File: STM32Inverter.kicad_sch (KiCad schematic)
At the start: 12 parts, among them U1 STM32F303VCTx, Y1 16MHz

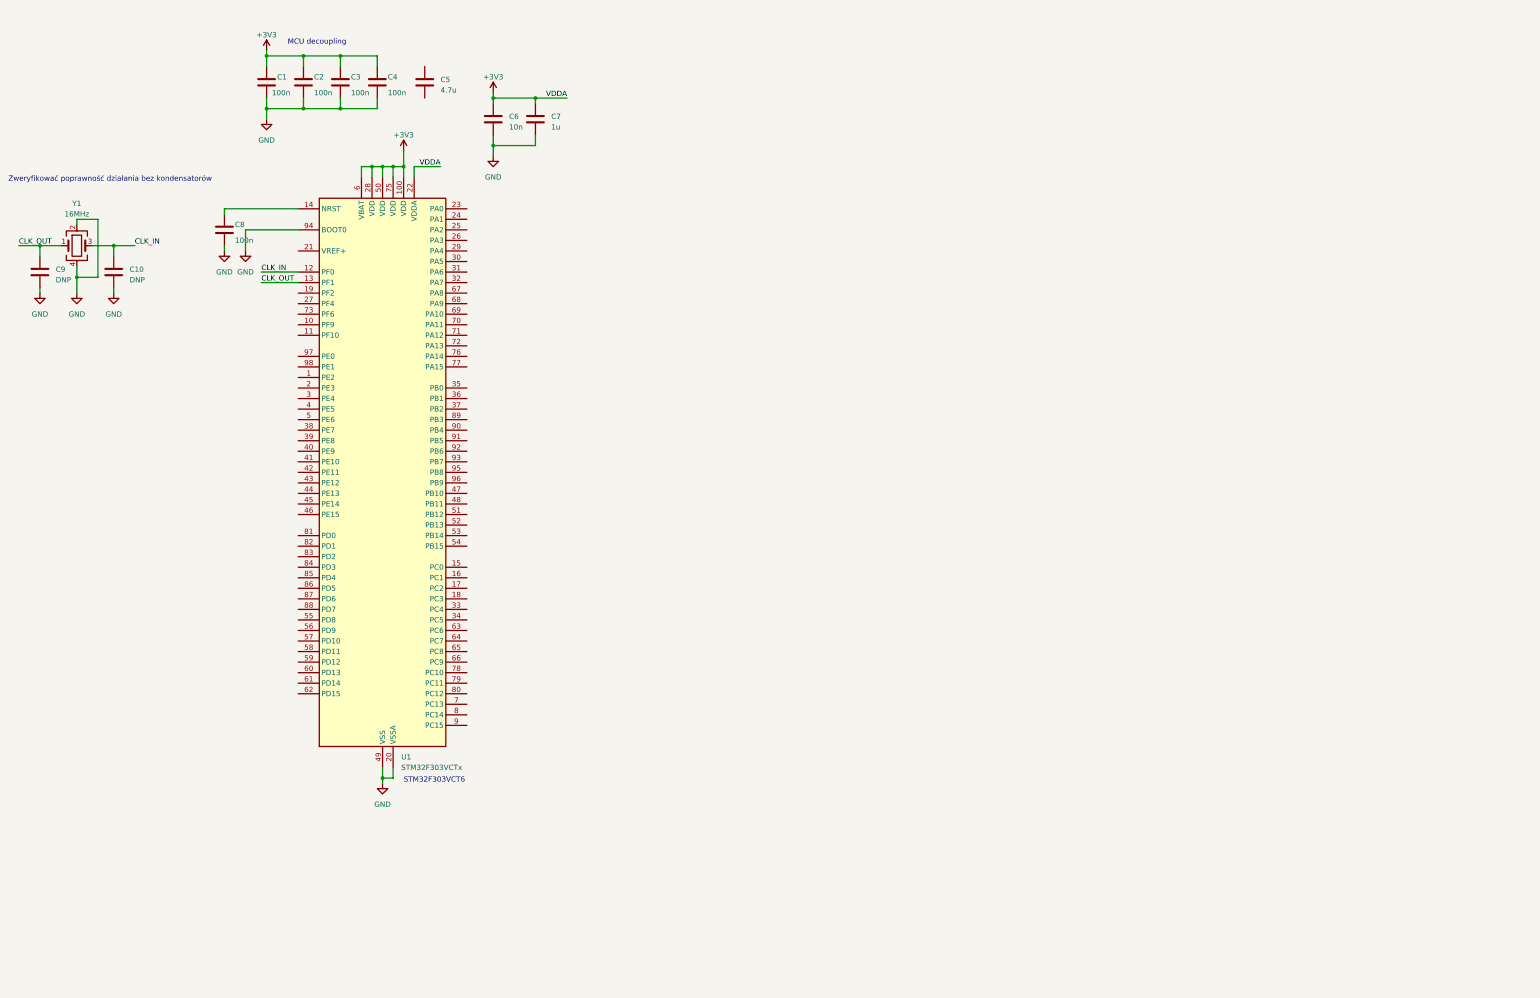
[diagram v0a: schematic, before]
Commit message: Added STM32Cube file and schematic subsheets
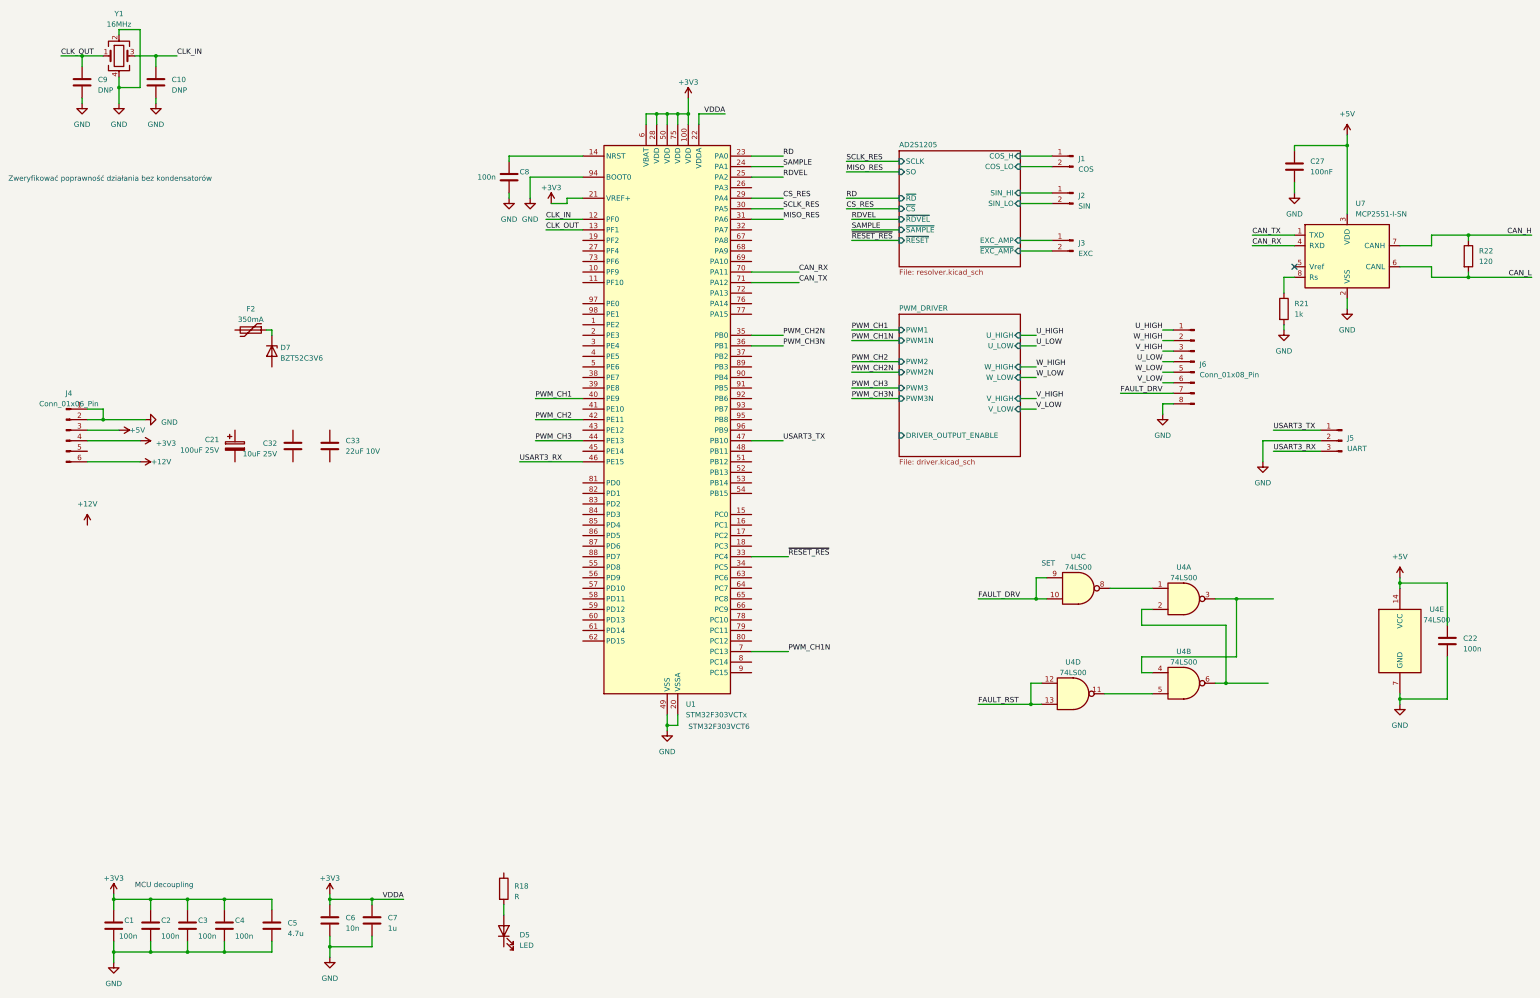
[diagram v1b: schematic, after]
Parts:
- added C21: 100uF 25V, Capacitor_SMD:CP_Elec_8x6.2, symbol Device:C_Polarized
- added C22: 100n, symbol Device:C
- added C27: 100nF, Capacitor_SMD:C_0603_1608Metric, symbol Device:C
- added C32: 10uF 25V, Capacitor_SMD:C_1206_3216Metric, symbol Device:C
- added C33: 22uF 10V, Capacitor_SMD:C_1206_3216Metric, symbol Device:C
- added D5: LED, symbol Device:LED
- added D7: BZT52C3V6, Diode_SMD:D_SOD-123, symbol Device:D_Zener
- added F2: 350mA, Fuse:Fuse_0805_2012Metric, symbol Device:Polyfuse
- added J1: COS, symbol Connector:Conn_01x02_Pin
- added J2: SIN, symbol Connector:Conn_01x02_Pin
- added J3: EXC, symbol Connector:Conn_01x02_Pin
- added J4: Conn_01x06_Pin, symbol Connector:Conn_01x06_Pin
- added J5: UART, symbol Connector:Conn_01x03_Pin
- added J6: Conn_01x08_Pin, symbol Connector:Conn_01x08_Pin
- added R18: R, symbol Device:R
- added R21: 1k, Resistor_SMD:R_0603_1608Metric, symbol Device:R
- added R22: 120, Resistor_SMD:R_0603_1608Metric, symbol Device:R
- added U4: 74LS00, symbol 74xx:74LS00
- added U7: MCP2551-I-SN, Package_SO:SOIC-8_3.9x4.9mm_P1.27mm, symbol Interface_CAN_LIN:MCP2551-I-SN
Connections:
- net +3V3: now also C5.1, U1.21 (VREF+), J4.4 (Pin_4)
- net GND: now also C5.2, C22.2, C27.2, J4.1 (Pin_1), J4.2 (Pin_2), J5.2 (Pin_2), J6.8 (Pin_8), R21.2, U4.7 (GND), U7.2 (VSS)
- net RD: now reaches U1.23 (PA0)
- net SAMPLE: now reaches U1.24 (PA1)
- net RDVEL: now reaches U1.25 (PA2)
- net CS_RES: now reaches U1.29 (PA4)
- net SCLK_RES: now reaches U1.30 (PA5)
- net MISO_RES: now reaches U1.31 (PA6)
- net ~{RESET_RES}: now reaches U1.33 (PC4)
- net PWM_CH2N: now reaches U1.35 (PB0)
- net PWM_CH3N: now reaches U1.36 (PB1)
- net PWM_CH1: now reaches U1.40 (PE9)
- net PWM_CH2: now reaches U1.42 (PE11)
- net PWM_CH3: now reaches U1.44 (PE13)
- net USART3_RX: now reaches U1.46 (PE15)
- net USART3_RX: now also J5.3 (Pin_3)
- net USART3_TX: now reaches U1.47 (PB10)
- net USART3_TX: now also J5.1 (Pin_1)
- net PWM_CH1N: now reaches U1.7 (PC13)
- net CAN_RX: now reaches U1.70 (PA11)
- net CAN_RX: now also U7.4 (RXD)
- net CAN_TX: now reaches U1.71 (PA12)
- net CAN_TX: now also U7.1 (TXD)
- new net: U4.3, U4.4
- new net: U4.11, U4.5
- new net: U4.2, U4.6
- new net: D7.1 (K), F2.1
- new net: U4.1, U4.8
- new net: D5.2 (A), R18.2
- new net: R21.1, U7.8 (Rs)
- new net +12V: J4.6 (Pin_6)
- new net +5V: C22.1, C27.1, J4.3 (Pin_3), U4.14 (VCC), U7.3 (VDD)
- new net AD2S1205/COS_H: J1.1 (Pin_1)
- new net AD2S1205/COS_LO: J1.2 (Pin_2)
- new net AD2S1205/EXC_AMP: J3.1 (Pin_1)
- new net AD2S1205/SIN_HI: J2.1 (Pin_1)
- new net AD2S1205/SIN_LO: J2.2 (Pin_2)
- new net AD2S1205/~{EXC_AMP}: J3.2 (Pin_2)
- new net CAN_H: R22.1, U7.7 (CANH)
- new net CAN_L: R22.2, U7.6 (CANL)
- new net FAULT_DRV: J6.7 (Pin_7), U4.10, U4.9
- new net FAULT_RST: U4.12, U4.13
- new net U_HIGH: J6.1 (Pin_1)
- new net U_LOW: J6.4 (Pin_4)
- new net V_HIGH: J6.3 (Pin_3)
- new net V_LOW: J6.6 (Pin_6)
- new net W_HIGH: J6.2 (Pin_2)
- new net W_LOW: J6.5 (Pin_5)
- no-connect marks 0 -> 1
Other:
- added sheet AD2S1205 (resolver.kicad_sch)
- added sheet PWM_DRIVER (driver.kicad_sch)
- note added: "SET"
- moved on the sheet: C1, C10, C2, C3, C4, C5, C6, C7, C8, C9, U1, Y1

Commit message: Added current sensing
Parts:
- removed C32: 10uF 25V, Capacitor_SMD:C_1206_3216Metric, symbol Device:C
- removed unit 3 of U4
- added C23: 22uF 10V, Capacitor_SMD:C_1206_3216Metric, symbol Device:C
- added D6: BZT52C3V6, Diode_SMD:D_SOD-123, symbol Device:D_Zener
- added F1: 350mA, Fuse:Fuse_0805_2012Metric, symbol Device:Polyfuse
- added J7: CURRENT SENSE, symbol Connector:Conn_01x04_Pin
- added R19: 4.7k, Resistor_SMD:R_0603_1608Metric, symbol Device:R
- added R20: 2.7k, Resistor_SMD:R_0603_1608Metric, symbol Device:R
- added R23, R24, R25, R26, R27, R28: 10k, symbol Device:R
- D7: value BZT52C3V6 -> BZT52C5V6
- J4: value Conn_01x06_Pin -> Power
- J6: value Conn_01x08_Pin -> DRIVER
- U4: value 74LS00 -> 74HCT00
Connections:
- net +12V: now also C21.1
- net +3V3: now also C23.1, D6.1 (K), F1.1; no longer J4.4 (Pin_4)
- net +5V: now also C33.1, D7.1 (K), F2.1, J7.1 (Pin_1), R23.1; no longer J4.3 (Pin_3)
- net FAULT_DRV: now also U4.1
- net GND: now also C21.2, C33.2, D5.1 (K), D7.2 (A), C23.2, D6.2 (A), J7.3 (Pin_3), R19.2, R24.2, R26.2, R28.2
- net at U4.3, U4.4: now also R20.1
- net at F2.2: now also J4.3 (Pin_3)
- net LED_PIN: now reaches R18.1
- new net: J7.4 (Pin_4), R25.1
- new net: J7.2 (Pin_2), R27.1
- new net: F1.2, J4.4 (Pin_4)
- new net 2.5V: R23.2, R24.1
- new net CURRENT_A: R27.2, R28.1
- new net CURRENT_B: R25.2, R26.1
- new net FAULT_SR_3V3: R19.1, R20.2
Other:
- sheet AD2S1205 ports: added DOS, LOT; removed none
- note added: "NOT DONE! ADD ENABLE VOLTAGE AND TEMP AND POWER!"
- note added: "PINS TO ARRANGE!!!"
- moved on the sheet: C21, C22, C27, C33, D7, F2, J1, J2, J3, J5, J6, R21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

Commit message: Connectors added
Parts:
- removed J1: COS, symbol Connector:Conn_01x02_Pin
- removed J2: SIN, symbol Connector:Conn_01x02_Pin
- removed J3: EXC, symbol Connector:Conn_01x02_Pin
- removed J6: DRIVER, symbol Connector:Conn_01x08_Pin
- added J1: INTERFACE, symbol Connector_Generic:Conn_02x10_Odd_Even
- added J2: RESOLVER, symbol Connector_Generic:Conn_02x06_Odd_Even
- added J6: RESOLVER, symbol Connector_Generic:Conn_02x10_Odd_Even
- added J8: DRIVER BOARD, symbol Connector_Generic:Conn_02x10_Odd_Even
- added R31, R32, R34, R36: 4.7k, Resistor_SMD:R_0603_1608Metric, symbol Device:R
- added R35: 2.7k, Resistor_SMD:R_0603_1608Metric, symbol Device:R
- added TP10, TP11, TP12, TP13, TP14, TP5, TP6, TP7, TP8, TP9: TestPoint, symbol Connector:TestPoint
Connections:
- net +5V: now also J1.12 (Pin_12), J8.17 (Pin_17), J8.19 (Pin_19)
- net CAN_H: now also J1.2 (Pin_2)
- net CAN_L: now also J1.4 (Pin_4)
- net FAULT_DRV: now also J8.4 (Pin_4)
- net GND: now also J1.10 (Pin_10), J2.12 (Pin_12), J8.7 (Pin_7), J8.9 (Pin_9), R31.2, R32.2, R34.2, R36.2
- net U_HIGH: now also J8.1 (Pin_1), TP9.1
- net U_LOW: now also J8.11 (Pin_11), TP10.1
- net V_HIGH: now also J8.5 (Pin_5), TP13.1
- net V_LOW: now also J8.15 (Pin_15), TP14.1
- net W_HIGH: now also J8.3 (Pin_3), TP11.1
- net W_LOW: now also J8.13 (Pin_13), TP12.1
- net +5VA: now reaches J4.5 (Pin_5)
- net +5VA: now also J8.2 (Pin_2)
- new net: J8.6 (Pin_6), TP8.1
- new net: J8.18 (Pin_18), TP6.1
- new net: J8.8 (Pin_8), R35.1
- new net: J8.16 (Pin_16), TP7.1
- new net: J8.20 (Pin_20), TP5.1
- new net ACC_INPUT_A: J1.6 (Pin_6)
- new net ACC_INPUT_B: J1.8 (Pin_8)
- new net BRK: J1.14 (Pin_14)
- new net KEY: J1.16 (Pin_16)
- new net T1_DRV: J8.10 (Pin_10), R34.1
- new net T2_DRV: J8.12 (Pin_12), R32.1
- new net T3_DRV: J8.14 (Pin_14), R31.1
- new net TG1: J2.4 (Pin_4)
- new net TG2: J2.8 (Pin_8)
- new net TH1: J2.6 (Pin_6)
- new net TH2: J2.10 (Pin_10)
- new net VBUS_DRV: R35.2, R36.1
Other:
- note added: "Add proper jellybeans"
- note added: "CHECK NTC TEMP RANGE"
- note added: "CHECK PINOUT"
- note added: "DIFFERENTIAL"
- note removed: "NOT DONE! ADD ENABLE VOLTAGE AND TEMP AND POWER!"
- moved on the sheet: R19, R20, U4A, U4B, U4D

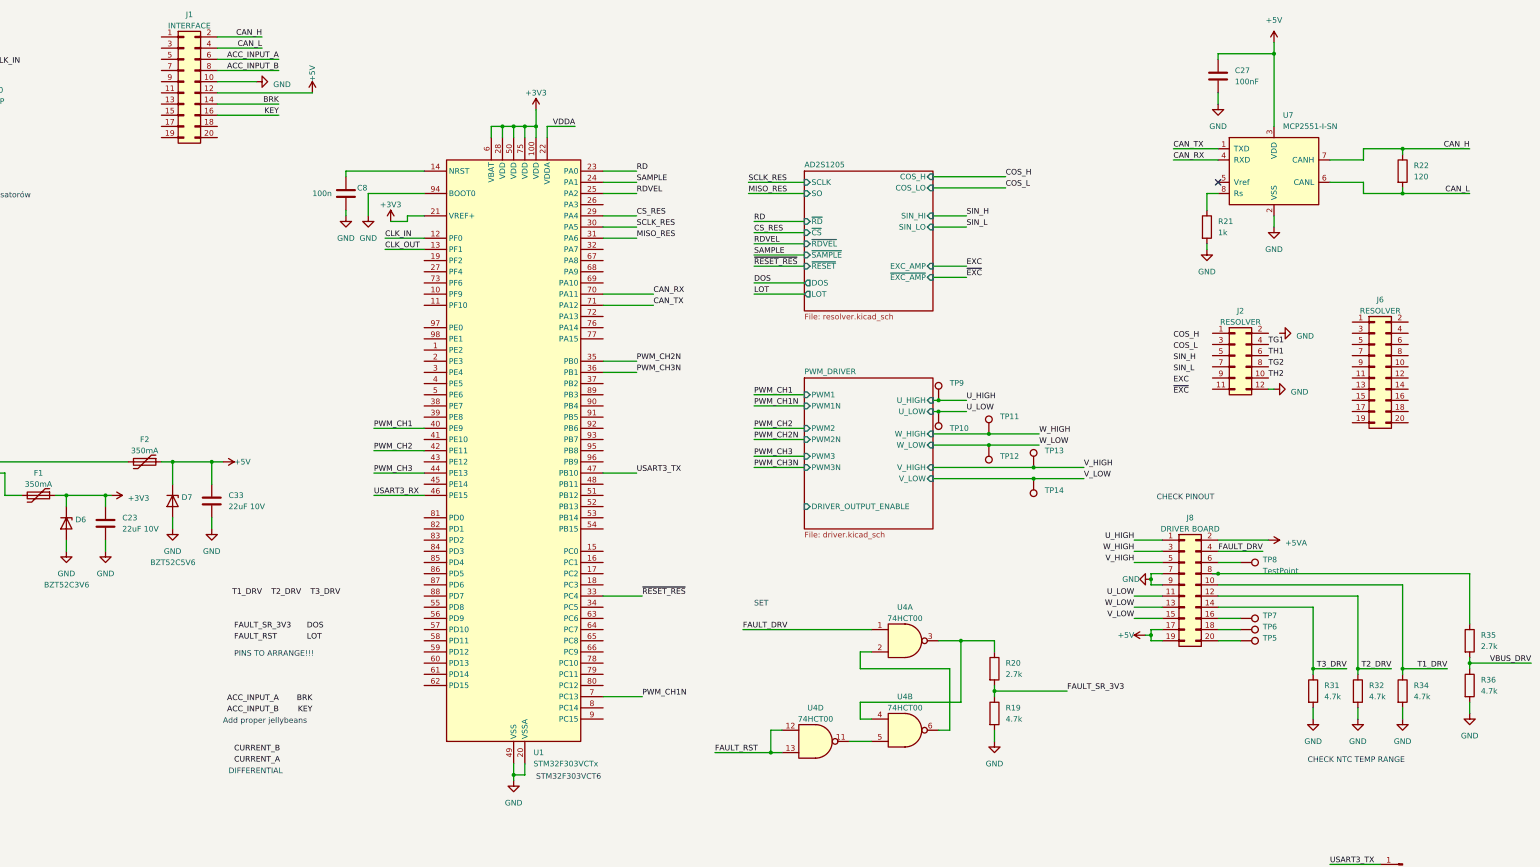
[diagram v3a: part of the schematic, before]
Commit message: Added some pin assignments
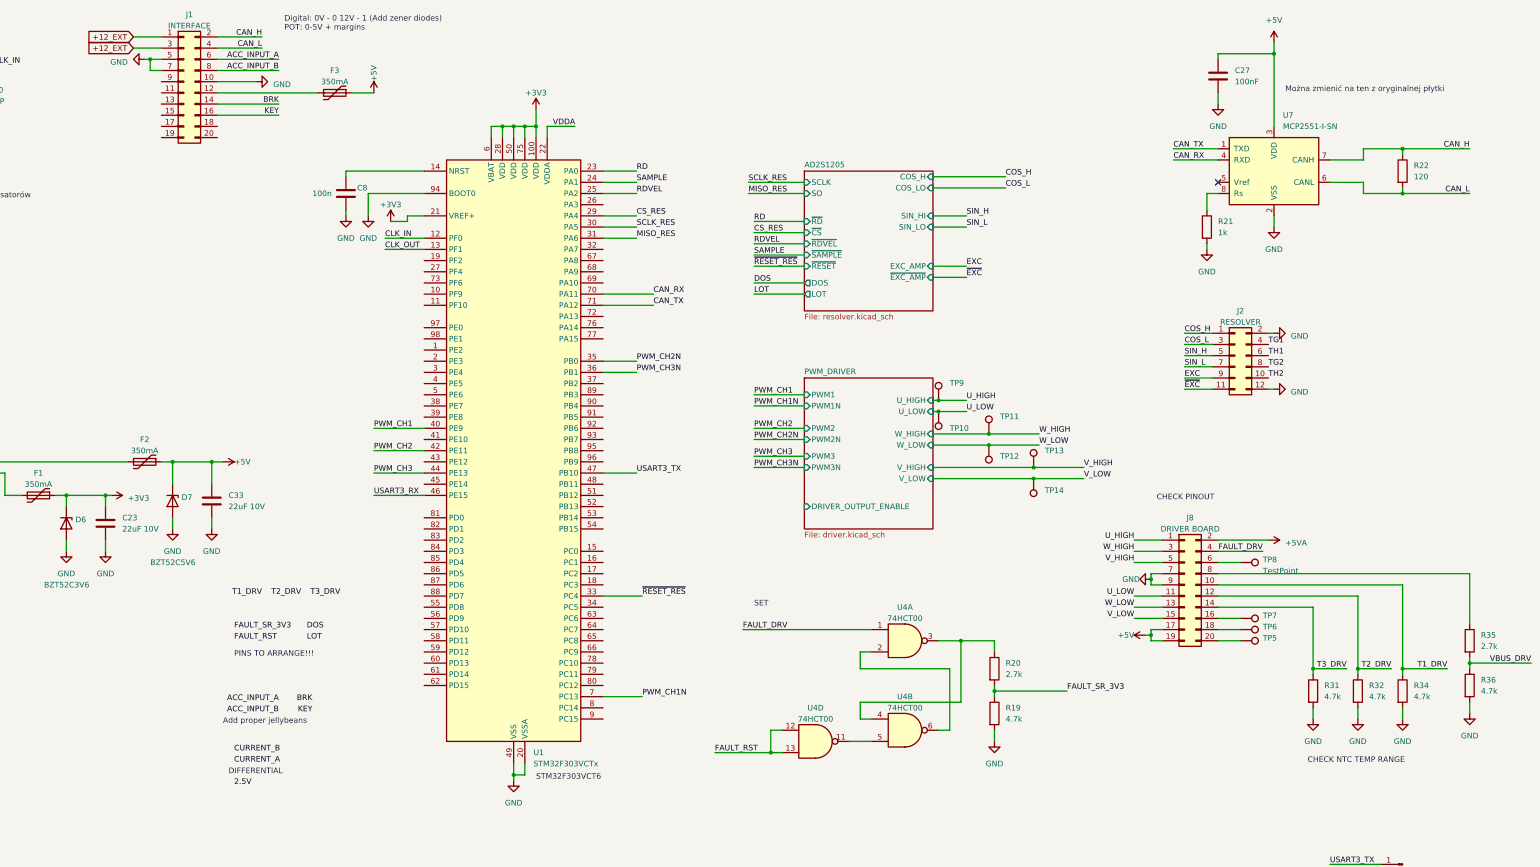
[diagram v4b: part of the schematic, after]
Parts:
- removed J6: RESOLVER, symbol Connector_Generic:Conn_02x10_Odd_Even
- added F3: 350mA, Fuse:Fuse_0805_2012Metric, symbol Device:Polyfuse
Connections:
- net +5V: now also F3.1; no longer J1.12 (Pin_12)
- net COS_H: now also J2.1 (Pin_1)
- net COS_L: now also J2.3 (Pin_3)
- net EXC: now also J2.9 (Pin_9)
- net GND: now also J1.5 (Pin_5), J1.7 (Pin_7), J2.2 (Pin_2)
- net SIN_H: now also J2.5 (Pin_5)
- net SIN_L: now also J2.7 (Pin_7)
- net ~{EXC}: now also J2.11 (Pin_11)
- net +12_EXT: now reaches J1.1 (Pin_1)
- net +12_EXT: now also J1.3 (Pin_3)
- new net: F3.2, J1.12 (Pin_12)
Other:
- note added: "Digital: 0V - 0 12V - 1 (Add zener diodes) POT: 0-5V + margins"
- note added: "Można zmienić na ten z oryginalnej płytki"

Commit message: Preliminary footprints
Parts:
- removed Y1: 16MHz, Oscillator:Oscillator_SMD_Abracon_ASDMB-4Pin_2.5x2.0mm, symbol MEMS_Passive:Crystal_16MHz_ECS-160-8-36CKM-TR3
- added Y3: CSTNE8M00GH5C000R0, Crystal:Resonator_SMD_Murata_CSTxExxV-3Pin_3.0x1.1mm_HandSoldering, symbol Device:Crystal_GND2
- C1, C2, C22, C3, C4: value 100n -> 1u; footprint (none) -> Capacitor_SMD:C_0402_1005Metric_Pad0.74x0.62mm_HandSolder; LCSC (none) -> C126521
- C10, C6, C8, C9: footprint (none) -> Capacitor_SMD:C_0603_1608Metric_Pad1.08x0.95mm_HandSolder
- C23, C33: LCSC (none) -> C920963
- C5: value 4.7u -> 1u; footprint (none) -> Capacitor_SMD:C_0402_1005Metric_Pad0.74x0.62mm_HandSolder; LCSC (none) -> C126521
- C7: footprint (none) -> Capacitor_SMD:C_0402_1005Metric_Pad0.74x0.62mm_HandSolder; LCSC (none) -> C126521
- D5, J1: footprint (none) -> LED_SMD:LED_0805_2012Metric_Pad1.15x1.40mm_HandSolder
- J2: footprint (none) -> Connector_IDC:IDC-Header_2x06_P2.54mm_Horizontal
- J4: footprint (none) -> Connector_IDC:IDC-Header_2x03_P2.54mm_Horizontal
- J5: footprint (none) -> Connector_PinHeader_2.54mm:PinHeader_1x03_P2.54mm_Vertical
- J7: footprint (none) -> Connector_JST:JST_PH_B4B-PH-K_1x04_P2.00mm_Vertical
- J8: footprint (none) -> Connector_IDC:IDC-Header_2x10_P2.54mm_Horizontal
- R18, R23, R24, R25, R26, R27, R28: footprint (none) -> Resistor_SMD:R_0603_1608Metric_Pad0.98x0.95mm_HandSolder
- TP10, TP11, TP12, TP13, TP14, TP5, TP6, TP7, TP8, TP9: footprint (none) -> TestPoint:TestPoint_Pad_D1.0mm
- U1: LCSC (none) -> C40764
- U4: footprint (none) -> Package_SO:SOIC-14_3.9x8.7mm_P1.27mm; LCSC (none) -> MM74HCT00M
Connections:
- net CLK_IN: now also Y3.3
- net CLK_OUT: now also Y3.1
- net GND: now also Y3.2
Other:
- moved on the sheet: U4E

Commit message: A lot of changes
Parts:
- removed J1: INTERFACE, LED_SMD:LED_0805_2012Metric_Pad1.15x1.40mm_HandSolder, symbol Connector_Generic:Conn_02x10_Odd_Even
- added D4: 1N4007, Diode_SMD:D_SMA_Handsoldering, symbol Device:D
- added F4: 2A, symbol Device:Fuse
- added J1: STLINK, symbol Connector:Conn_01x04_Pin
- added J3: MAIN POWER, symbol Connector:Conn_01x02_Pin
- added J6: INTERFACE, Connector_IDC:IDC-Header_2x08_P2.54mm_Vertical, symbol Connector_Generic:Conn_02x08_Odd_Even
- added R29: 2.7k, Resistor_SMD:R_0603_1608Metric, symbol Device:R
- added R30: 4.7k, Resistor_SMD:R_0603_1608Metric, symbol Device:R
- D6: LCSC (none) -> C2891771
- D7: LCSC (none) -> C2119
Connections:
- net +12_EXT: now also F4.1, J6.1 (Pin_1), J6.3 (Pin_3)
- net +3V3: now also J1.1 (Pin_1)
- net ACC_INPUT_A: now also J6.6 (Pin_6)
- net ACC_INPUT_B: now also J6.8 (Pin_8)
- net BRK: now also J6.14 (Pin_14)
- net CAN_H: now also J6.2 (Pin_2)
- net CAN_L: now also J6.4 (Pin_4)
- net GND: now also D4.2 (A), J1.4 (Pin_4), J3.2 (Pin_2), J6.10 (Pin_10), J6.5 (Pin_5), J6.7 (Pin_7), R30.2
- net KEY: now also J6.16 (Pin_16)
- net at F3.2: now also J6.12 (Pin_12)
- net SWDIO: now reaches U1.72 (PA13)
- net SWDIO: now also J1.2 (Pin_2)
- net SWCLK: now reaches U1.76 (PA14)
- net SWCLK: now also J1.3 (Pin_3)
- new net: D4.1 (K), F4.2, J3.1 (Pin_1), R29.1
- new net +12_EXT_ADC: R29.2, R30.1
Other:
- company: (none) -> WZS
- moved on the sheet: C10, C21, C22, C23, C27, C33, C9, D5, D6, D7, F1, F2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
